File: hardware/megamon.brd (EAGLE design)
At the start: 100 x 55.9 mm, 75 parts

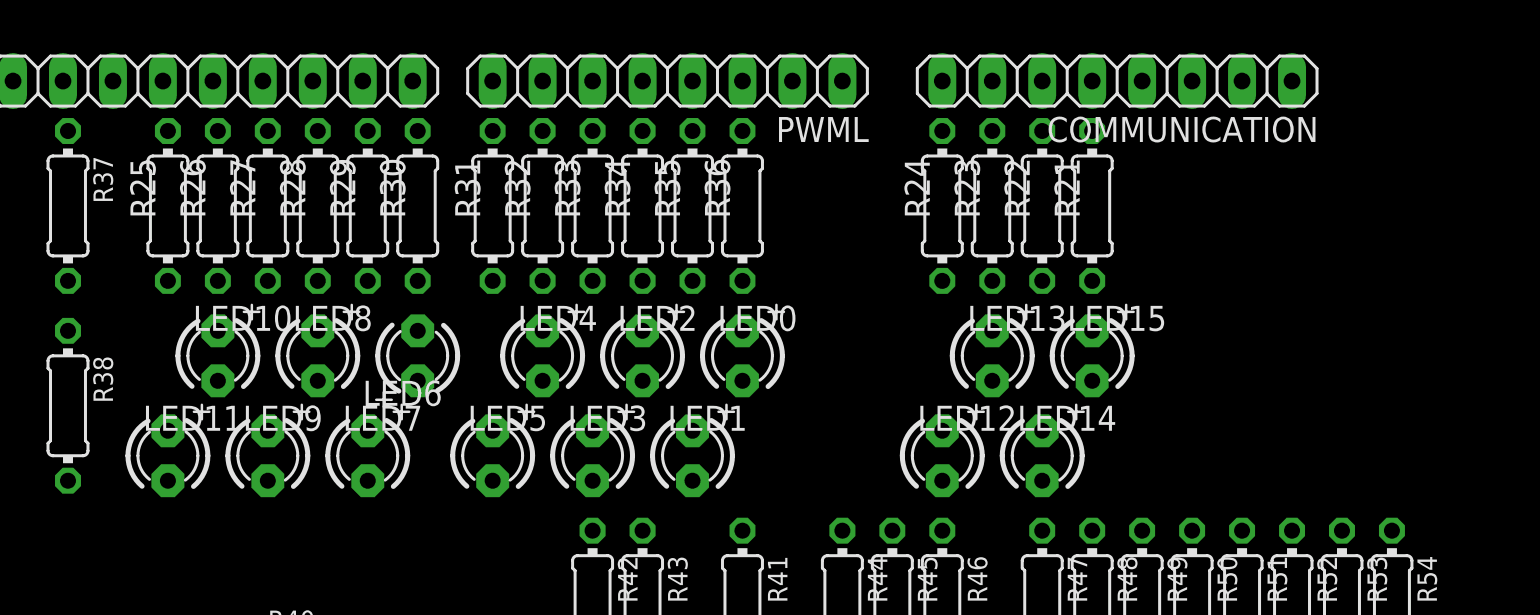
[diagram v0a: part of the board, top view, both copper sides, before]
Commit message: removed all but one LED
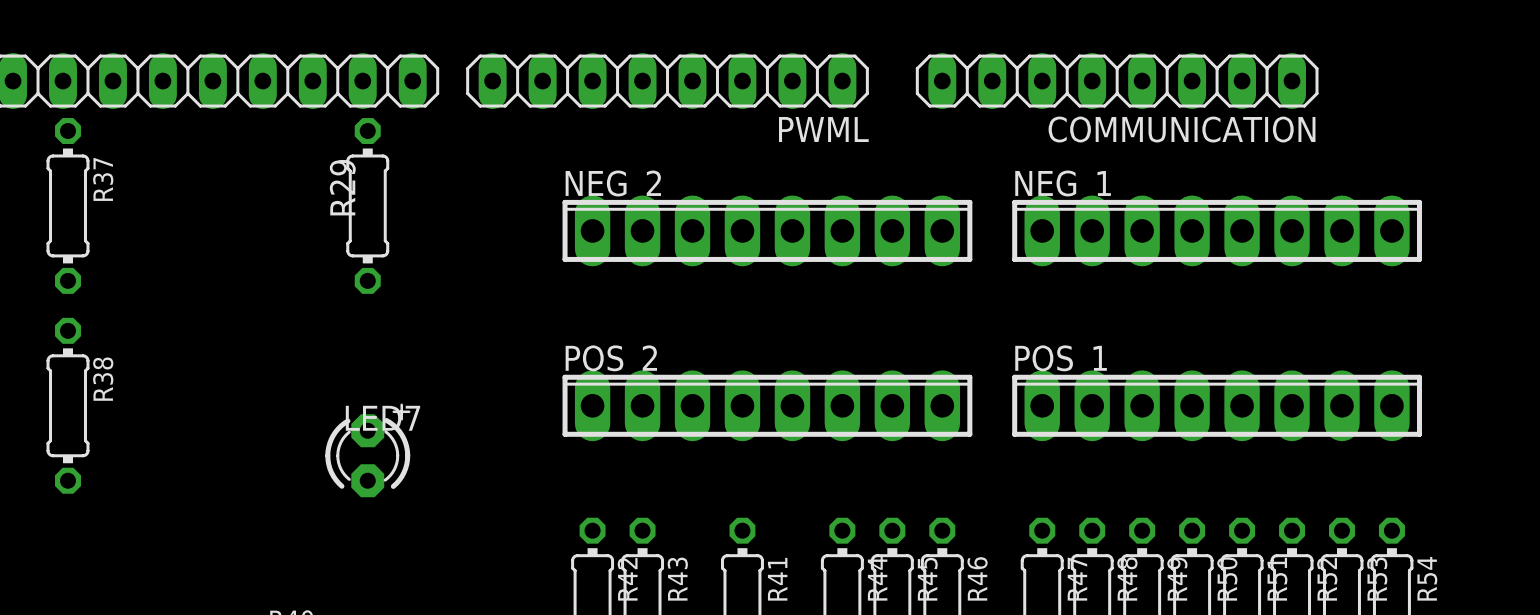
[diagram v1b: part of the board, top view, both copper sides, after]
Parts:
- removed LED0, LED1, LED10, LED11, LED12, LED13, LED14, LED15, LED2, LED3, LED4, LED5, LED6, LED8, LED9: green, adafruit:LED3MM
- removed R21, R22, R23, R24, R25, R26, R27, R28, R30, R31, R32, R33, R34, R35, R36: 1K, rcl:0204/7
- added NEG_1, NEG_2, POS_1, POS_2: (no value), con-phoenix-254:8POL254
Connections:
- removed net D10: JP6.8, R28.2
- removed net D11: JP6.7, R27.2
- removed net D12: JP6.6, R26.2
- removed net D13: JP6.5, R25.2
- removed net D14: COMMUNICATION.8, R24.2
- removed net D15: COMMUNICATION.7, R23.2
- removed net D16: COMMUNICATION.6, R22.2
- removed net D17: COMMUNICATION.5, R21.2
- removed net D2: PWML.3, R36.2
- removed net D3: PWML.4, R35.2
- removed net D4: PWML.5, R34.2
- removed net D5: PWML.6, R33.2
- removed net D6: PWML.7, R32.2
- removed net D7: PWML.8, R31.2
- removed net D8: JP6.10, R30.2
- removed net N$10: LED8.A, R28.1
- removed net N$12: LED6.A, R30.1
- removed net N$13: LED5.A, R31.1
- removed net N$14: LED4.A, R32.1
- removed net N$15: LED3.A, R33.1
- removed net N$16: LED2.A, R34.1
- removed net N$17: LED1.A, R35.1
- removed net N$18: LED0.A, R36.1
- removed net N$3: LED14.A, R22.1
- removed net N$4: LED13.A, R23.1
- removed net N$41: LED15.A, R21.1
- removed net N$5: LED12.A, R24.1
- removed net N$7: LED11.A, R25.1
- removed net N$8: LED10.A, R26.1
- removed net N$9: LED9.A, R27.1
- net GND: no longer LED0.K, LED1.K, LED10.K, LED11.K, LED12.K, LED13.K, LED14.K, LED15.K, LED2.K, LED3.K, LED4.K, LED5.K, LED6.K, LED8.K, LED9.K

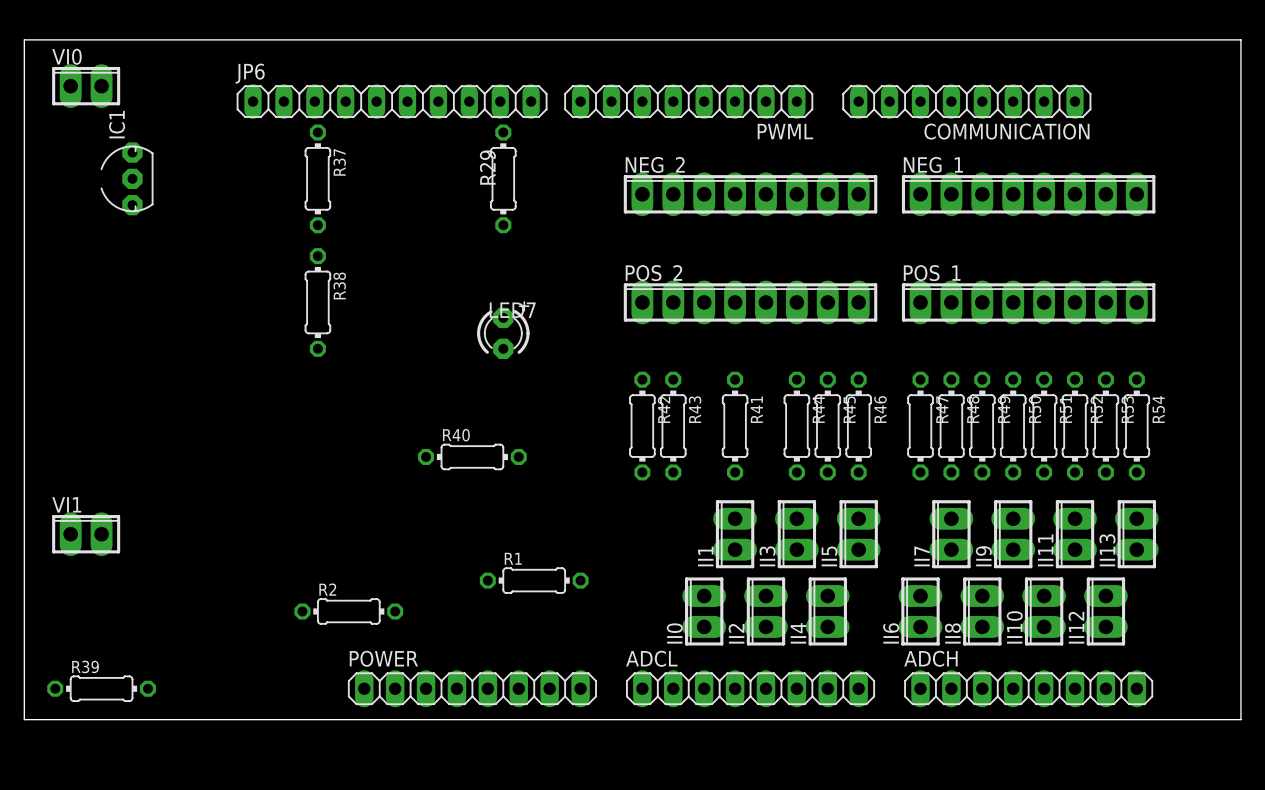
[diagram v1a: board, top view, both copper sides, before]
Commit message: replace pair terminals with separate pos/neg
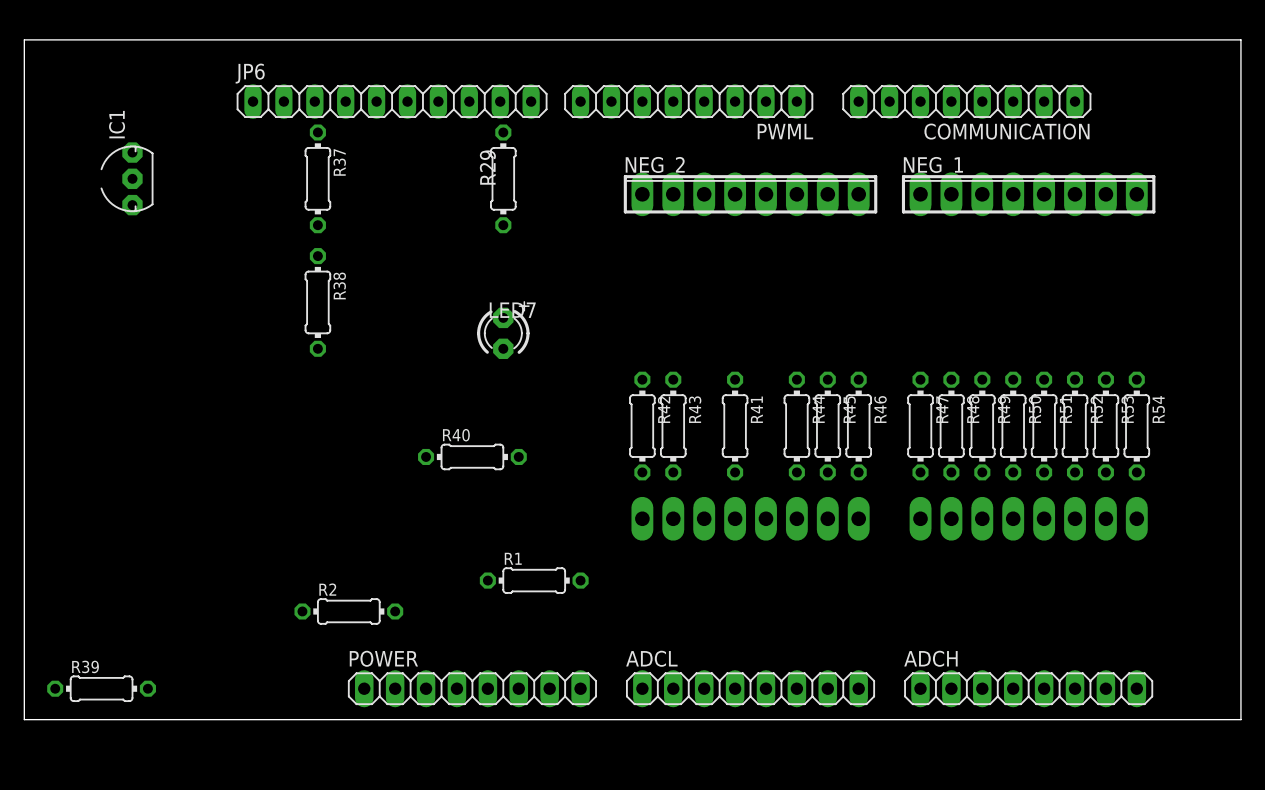
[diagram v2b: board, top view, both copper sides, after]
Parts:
- removed II0, II1, II10, II11, II12, II13, II2, II3, II4, II5, II6, II7, II8, II9, VI0, VI1: (no value), con-phoenix-254:2POL254
- moved POS_1 29.0 mm to (59.7, 16.5), flipped to the bottom
- moved POS_2 29.0 mm to (82.5, 16.5), flipped to the bottom
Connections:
- net ADC10: now also POS_2.6; no longer II8.1
- net ADC11: now also POS_2.5; no longer II9.1
- net ADC12: now also POS_2.4; no longer II10.1
- net ADC13: now also POS_2.3; no longer II11.1
- net ADC14: now also POS_2.2; no longer II12.1
- net ADC15: now also POS_2.1; no longer II13.1
- net ADC2: now also POS_1.6; no longer II0.1
- net ADC3: now also POS_1.5; no longer II1.1
- net ADC4: now also POS_1.4; no longer II2.1
- net ADC5: now also POS_1.3; no longer II3.1
- net ADC6: now also POS_1.2; no longer II4.1
- net ADC7: now also POS_1.1; no longer II5.1
- net ADC8: now also POS_2.8; no longer II6.1
- net ADC9: now also POS_2.7; no longer II7.1
- net N$2: now also POS_1.7; no longer VI1.1
- net N$6: now also POS_1.8; no longer VI0.1
- net V_MID: now also NEG_1.1, NEG_1.2, NEG_1.3, NEG_1.4, NEG_1.5, NEG_1.6, NEG_1.7, NEG_1.8, NEG_2.1, NEG_2.2, NEG_2.3, NEG_2.4, NEG_2.5, NEG_2.6, NEG_2.7, NEG_2.8; no longer II0.2, II1.2, II10.2, II11.2, II12.2, II13.2, II2.2, II3.2, II4.2, II5.2, II6.2, II7.2, II8.2, II9.2, VI0.2, VI1.2

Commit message: component placement done
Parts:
- moved R39 51.5 mm to (55.9, 16.5), turned to 270 degrees
- moved IC1 46.0 mm to (38.1, 8.89), turned to 180 degrees
- moved R2 35.1 mm to (61.0, 16.5), turned to 270 degrees
- moved R1 17.3 mm to (58.4, 16.5), turned to 270 degrees
- moved R40 17.3 mm to (53.3, 16.5), turned to 90 degrees
- moved R38 11.1 mm to (33.9, 29.1)
- moved R37 9.99 mm to (33.9, 42.4)
- moved POS_1 7.62 mm to (59.7, 8.89)
- moved POS_2 7.62 mm to (82.5, 8.89)
- moved R42 7.62 mm to (50.8, 16.5), turned to 90 degrees
- moved R44 7.62 mm to (63.5, 16.5)
- moved R45 7.62 mm to (66.0, 16.5)
- moved R46 7.62 mm to (68.6, 16.5)
- moved R47 7.62 mm to (73.7, 16.5)
- moved R48 7.62 mm to (76.2, 16.5)
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
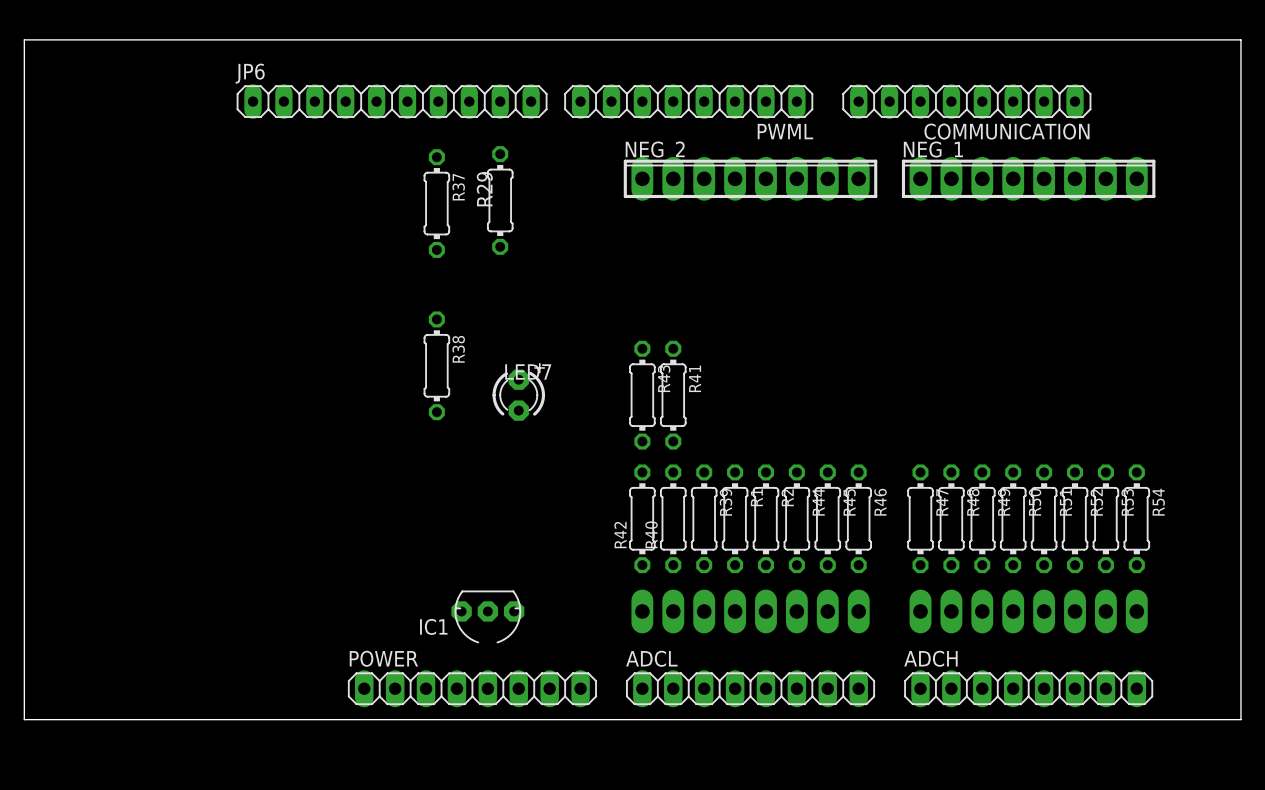
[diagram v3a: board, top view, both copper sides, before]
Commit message: traces done, gnd plane done
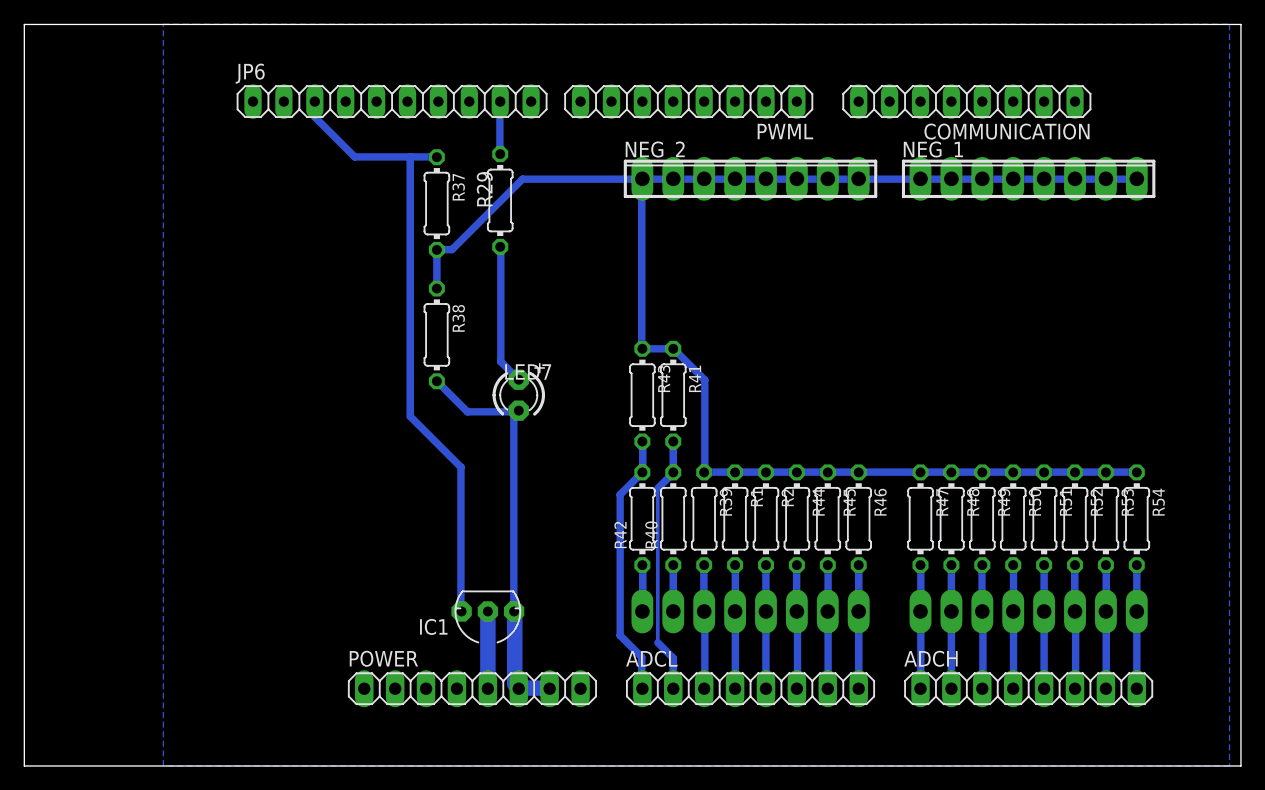
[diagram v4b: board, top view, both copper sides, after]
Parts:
- moved R38 2.54 mm to (33.9, 31.6)
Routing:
- net V_MID: track 0.00 -> 127.1 mm
- net AREF: track 0.00 -> 51.8 mm
- net GND: track 0.00 -> 33.7 mm
- net ADC0: track 0.00 -> 21.9 mm
- net ADC1: track 0.00 -> 21.4 mm
- net N$11: track 0.00 -> 11.6 mm
- net ADC10: track 0.00 -> 10.2 mm
- net ADC5: track 0.00 -> 10.2 mm
- net ADC2: track 0.00 -> 10.2 mm
- net ADC13: track 0.00 -> 10.2 mm
- net ADC8: track 0.00 -> 10.2 mm
- net ADC11: track 0.00 -> 10.2 mm
- net ADC3: track 0.00 -> 10.2 mm
- net ADC6: track 0.00 -> 10.2 mm
- net ADC14: track 0.00 -> 10.2 mm
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- added copper zone on layer 16, net GND
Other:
- board size 100 x 55.9 mm -> 100 x 61 mm
